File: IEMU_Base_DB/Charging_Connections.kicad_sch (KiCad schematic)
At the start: 57 parts, among them J201 DF13-4P-1.25H_51_, J202 DF13-4P-1.25H_51_, J203 DF13-4P-1.25H_51_, J204 DF13-4P-1.25H_51_, U201 TPS2553DRVT, U202 TPS2553DRVT, U203 TPS2553DRVT, U204 TPS2553DRVT

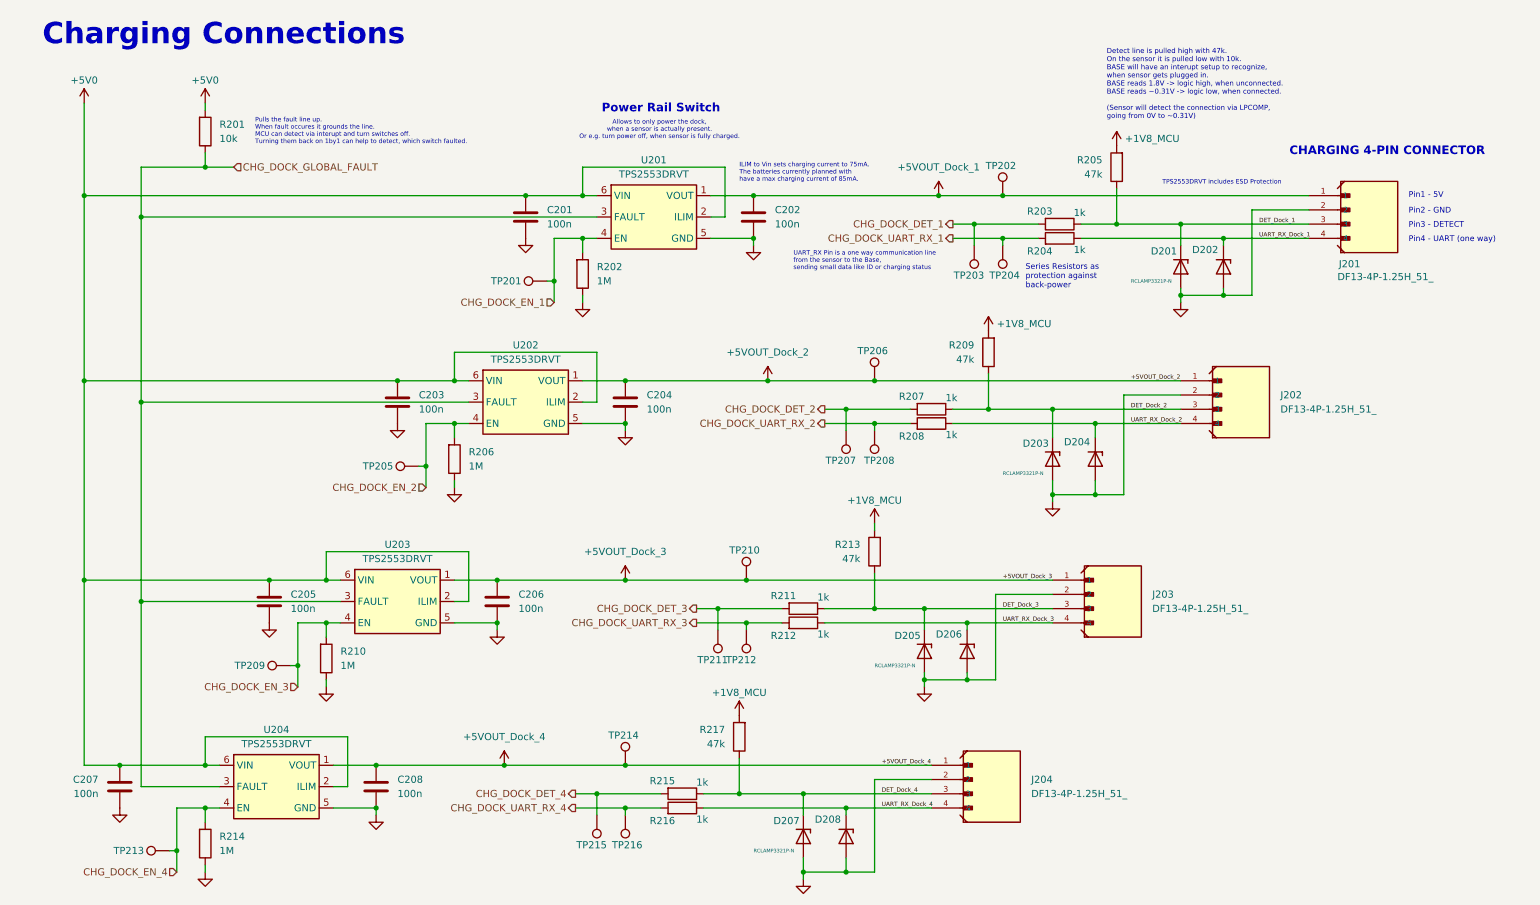
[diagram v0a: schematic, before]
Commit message: implemented changes from the review with TF and fixed lost parts in the library
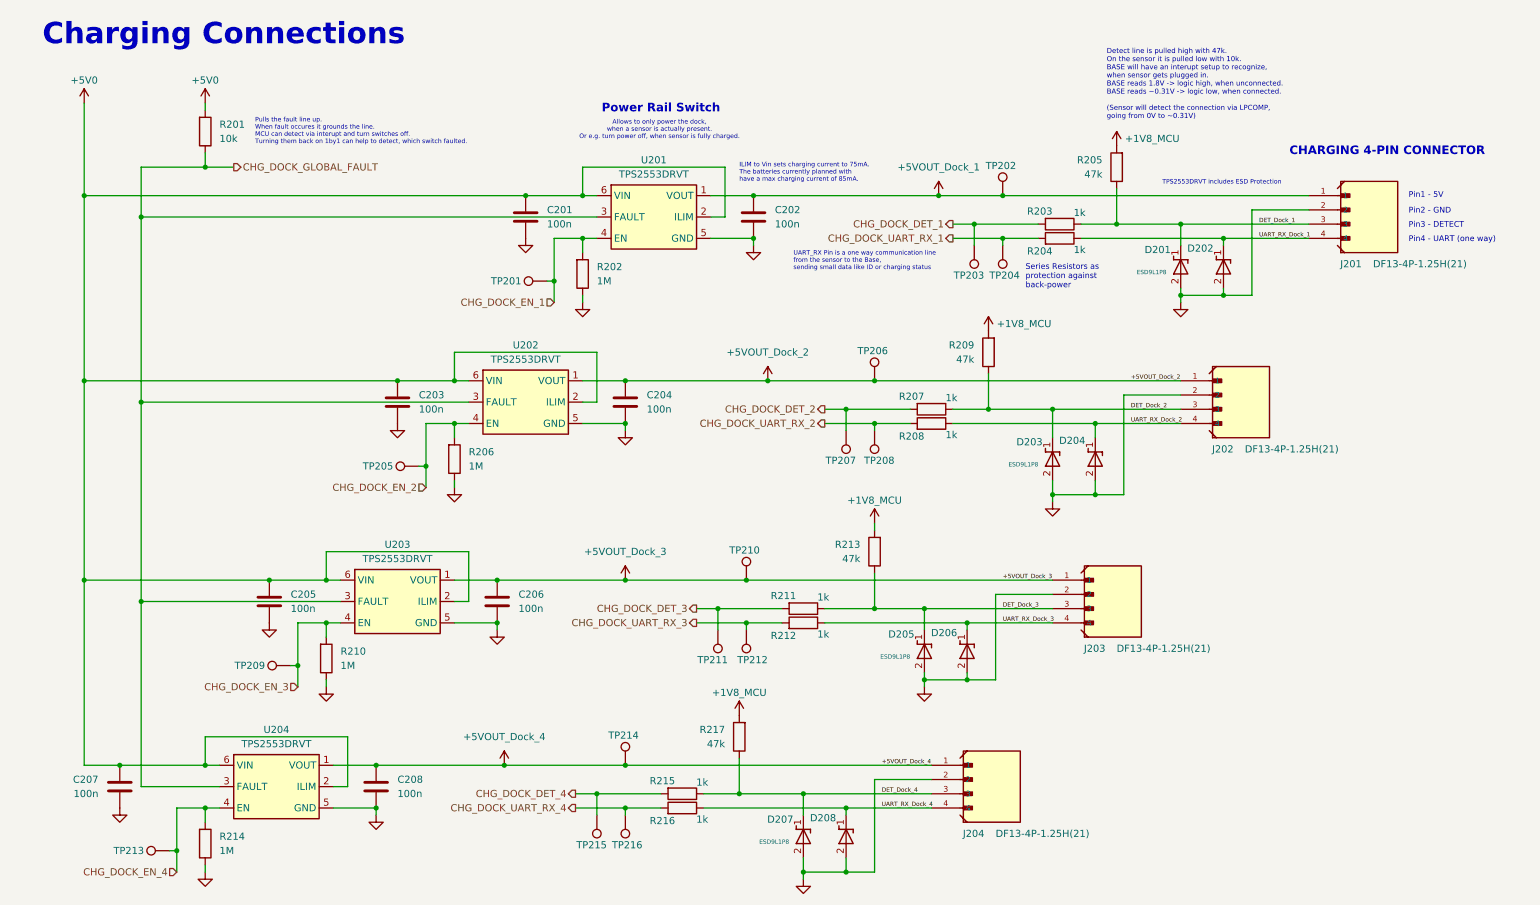
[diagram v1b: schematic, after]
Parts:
- removed D201, D202, D203, D204, D205, D206, D207, D208: RCLAMP3321P-N, Diode_SMD:D_SOD-882, symbol 0_Connectors:RCLAMP3321P-N
- removed J201, J202, J203, J204: DF13-4P-1.25H_51_, 0_Connectors:HRS_DF13-4P-1.25H_75_, symbol 0_Connectors:DF13-4P-1.25H_75_
- added D201, D202, D203, D204, D205, D206, D207, D208: ESD9L1P8, Diode_SMD:D_SOD-882, symbol 0_Power:ESD9L1P8
- added J201, J202, J203, J204: DF13-4P-1.25H(21), 0_Connectors:DF13-4P-1.25H(21), symbol 0_Connectors:DF13-4P-1.25H(21)
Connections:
- net +5VOUT_Dock_1: now also J201.1
- net +5VOUT_Dock_2: now also J202.1
- net +5VOUT_Dock_3: now also J203.1
- net +5VOUT_Dock_4: now also J204.1
- net DET_Dock_1: now also D201.1 (I/O), J201.3
- net DET_Dock_2: now also D203.1 (I/O), J202.3
- net DET_Dock_3: now also D205.1 (I/O), J203.3
- net DET_Dock_4: now also D207.1 (I/O), J204.3
- net GND: now also D201.2 (GND), D202.2 (GND), D203.2 (GND), D204.2 (GND), D205.2 (GND), D206.2 (GND), D207.2 (GND), D208.2 (GND), J201.2, J202.2, J203.2, J204.2
- net UART_RX_Dock_1: now also D202.1 (I/O), J201.4
- net UART_RX_Dock_2: now also D204.1 (I/O), J202.4
- net UART_RX_Dock_3: now also D206.1 (I/O), J203.4
- net UART_RX_Dock_4: now also D208.1 (I/O), J204.4

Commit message: layout of base and some fixes on the sensor layout
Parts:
- TP201, TP202, TP203, TP204, TP205, TP206, TP207, TP208, TP209, TP210, TP211, TP212, TP213, TP214, TP215, TP216: footprint TestPoint:TestPoint_Pad_D2.0mm -> TestPoint:TestPoint_Pad_D1.0mm
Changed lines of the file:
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@@
 			)
 		)
-		(property "Footprint" "TestPoint:TestPoint_Pad_D2.0mm"
+		(property "Footprint" "TestPoint:TestPoint_Pad_D1.0mm"
 			(at 116.84 158.75 0)
 			(effects
@@
 			)
 		)
-		(property "Footprint" "TestPoint:TestPoint_Pad_D2.0mm"
+		(property "Footprint" "TestPoint:TestPoint_Pad_D1.0mm"
 			(at 171.45 81.28 0)
 			(effects
@@
 			)
 		)
-		(property "Footprint" "TestPoint:TestPoint_Pad_D2.0mm"
+		(property "Footprint" "TestPoint:TestPoint_Pad_D1.0mm"
 			(at 62.23 137.16 0)
 			(effects
@@
 			)
 		)
-		(property "Footprint" "TestPoint:TestPoint_Pad_D2.0mm"
+		(property "Footprint" "TestPoint:TestPoint_Pad_D1.0mm"
 			(at 161.29 90.17 0)
 			(effects
@@
 			)
 		)
-		(property "Footprint" "TestPoint:TestPoint_Pad_D2.0mm"
+		(property "Footprint" "TestPoint:TestPoint_Pad_D1.0mm"
 			(at 156.21 90.17 0)
 			(effects
@@
 			)
 		)
-		(property "Footprint" "TestPoint:TestPoint_Pad_D2.0mm"
+		(property "Footprint" "TestPoint:TestPoint_Pad_D1.0mm"
 			(at 184.15 57.15 0)
 			(effects
@@
 			)
 		)
-		(property "Footprint" "TestPoint:TestPoint_Pad_D2.0mm"
+		(property "Footprint" "TestPoint:TestPoint_Pad_D1.0mm"
 			(at 148.59 116.84 0)
 			(effects
@@
 			)
 		)
-		(property "Footprint" "TestPoint:TestPoint_Pad_D2.0mm"
+		(property "Footprint" "TestPoint:TestPoint_Pad_D1.0mm"
 			(at 107.95 68.58 0)
 			(effects
@@
 			)
 		)
-		(property "Footprint" "TestPoint:TestPoint_Pad_D2.0mm"
+		(property "Footprint" "TestPoint:TestPoint_Pad_D1.0mm"
 			(at 127 149.86 0)
 			(effects
@@
 			)
 		)
-		(property "Footprint" "TestPoint:TestPoint_Pad_D2.0mm"
+		(property "Footprint" "TestPoint:TestPoint_Pad_D1.0mm"
 			(at 133.35 125.73 0)
 			(effects
@@
 			)
 		)
-		(property "Footprint" "TestPoint:TestPoint_Pad_D2.0mm"
+		(property "Footprint" "TestPoint:TestPoint_Pad_D1.0mm"
 			(at 40.64 170.18 0)
 			(effects
@@
 			)
 		)
-		(property "Footprint" "TestPoint:TestPoint_Pad_D2.0mm"
+		(property "Footprint" "TestPoint:TestPoint_Pad_D1.0mm"
 			(at 138.43 125.73 0)
 			(effects
@@
 			)
 		)
-		(property "Footprint" "TestPoint:TestPoint_Pad_D2.0mm"
+		(property "Footprint" "TestPoint:TestPoint_Pad_D1.0mm"
 			(at 194.31 48.26 0)
 			(effects
@@
 			)
 		)
-		(property "Footprint" "TestPoint:TestPoint_Pad_D2.0mm"
+		(property "Footprint" "TestPoint:TestPoint_Pad_D1.0mm"
 			(at 85.09 101.6 0)
 			(effects
@@
 			)
 		)
-		(property "Footprint" "TestPoint:TestPoint_Pad_D2.0mm"
+		(property "Footprint" "TestPoint:TestPoint_Pad_D1.0mm"
 			(at 111.76 158.75 0)
 			(effects
@@
 			)
 		)
-		(property "Footprint" "TestPoint:TestPoint_Pad_D2.0mm"
+		(property "Footprint" "TestPoint:TestPoint_Pad_D1.0mm"
 			(at 179.07 57.15 0)
 			(effects
